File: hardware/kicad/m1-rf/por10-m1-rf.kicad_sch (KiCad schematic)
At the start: 17 parts, among them T1 1:5, U1 Si4735-D60-SSOP24, X1 32.768kHz

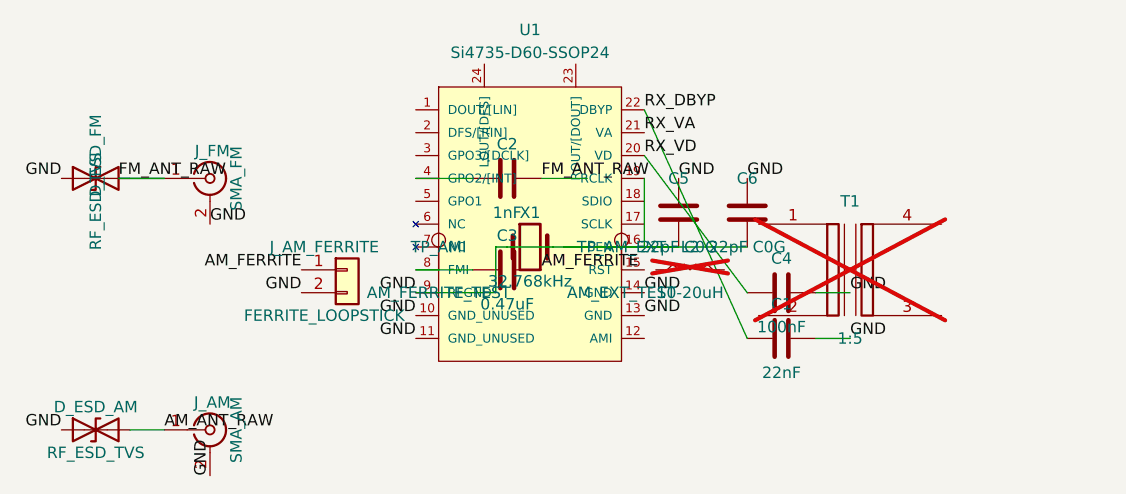
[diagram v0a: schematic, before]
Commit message: M1.3: add AM baseline bypass resistor
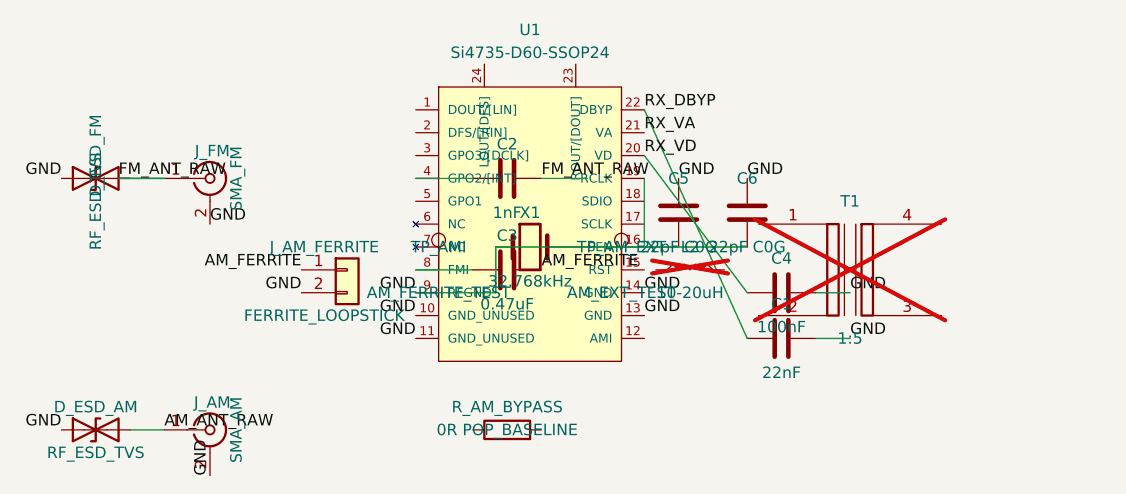
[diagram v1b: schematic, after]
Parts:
- added R_AM_BYPASS: 0R POP_BASELINE, symbol Device:R
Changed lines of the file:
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@@
     (effects (font (size 1.27 1.27)) (justify left bottom))
+  )
+  (symbol
+    (lib_id "Device:R")
+    (at 124.46 124.46 90)
+    (unit 1)
+    (exclude_from_sim no)
+    (in_bom yes)
+    (on_board yes)
+    (dnp no)
+    (property "Reference" "R_AM_BYPASS" (at 124.46 121.92 90) (effects (font (size 1.27 1.27))))
+    (property "Value" "0R POP_BASELINE" (at 124.46 124.46 90) (effects (font (size 1.27 1.27))))
+    (property "Footprint" "" (at 124.46 126.238 90) (effects (font (size 1.27 1.27)) (hide yes)))
+    (property "Datasheet" "~" (at 124.46 124.46 0) (effects (font (size 1.27 1.27)) (hide yes)))
+    (property "Description" "Q1 baseline 0-ohm bypass for external AM/SW matching experiments" (at 124.46 124.46 0) (effects (font (size 1.27 1.27)) (hide yes)))
+    (pin "1")
+    (pin "2")
+    (instances (project "por10-m1-rf" (path "/2b0f5db7-74f4-4a9a-bfc8-7bcbf6f10a13" (reference "R_AM_BYPASS") (unit 1))))
   )
   (sheet_instances

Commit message: M1.3: connect AM baseline bypass to external test node
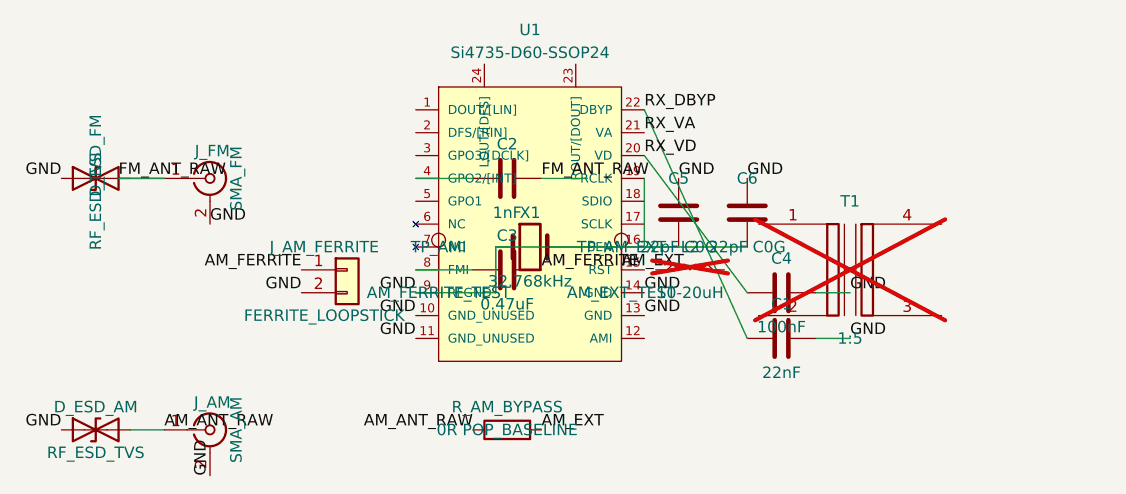
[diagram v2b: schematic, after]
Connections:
- net AM_ANT_RAW: now also R_AM_BYPASS.1
- net AM_EXT: now reaches TP_AM_EXT.1
- net AM_EXT: now also R_AM_BYPASS.2
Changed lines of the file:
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@@
     (instances (project "por10-m1-rf" (path "/2b0f5db7-74f4-4a9a-bfc8-7bcbf6f10a13" (reference "R_AM_BYPASS") (unit 1))))
+  )
+  (label "AM_ANT_RAW"
+    (at 120.65 124.46 180)
+    (effects (font (size 1.27 1.27)) (justify right bottom))
+  )
+  (label "AM_EXT"
+    (at 128.27 124.46 0)
+    (effects (font (size 1.27 1.27)) (justify left bottom))
+  )
+  (label "AM_EXT"
+    (at 137.16 106.68 0)
+    (effects (font (size 1.27 1.27)) (justify left bottom))
   )
   (sheet_instances

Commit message: M1.3: add selectable external AM link
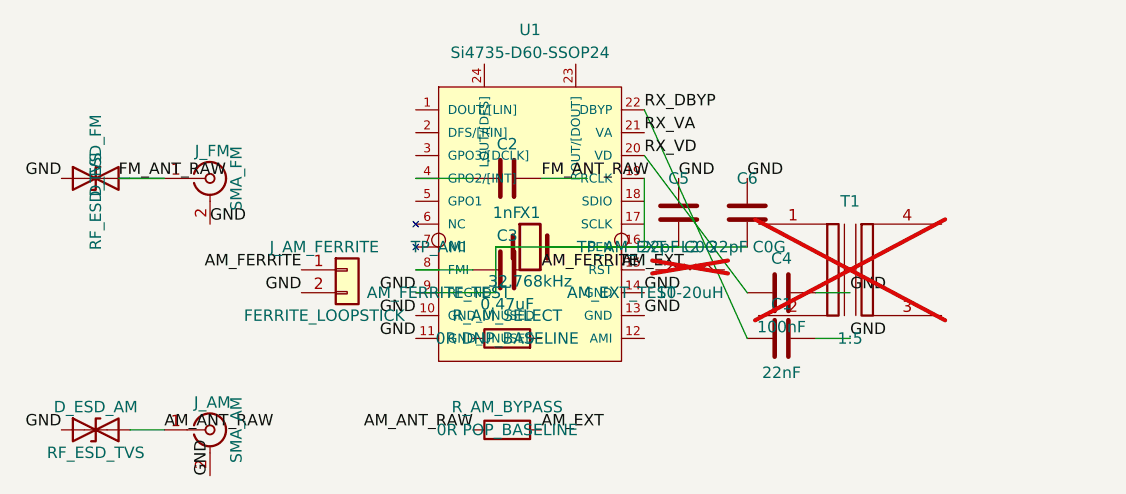
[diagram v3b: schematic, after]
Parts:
- added R_AM_SELECT: 0R DNP_BASELINE, symbol Device:R
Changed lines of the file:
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@@
     (effects (font (size 1.27 1.27)) (justify left bottom))
+  )
+  (symbol
+    (lib_id "Device:R")
+    (at 124.46 114.3 90)
+    (unit 1)
+    (exclude_from_sim no)
+    (in_bom yes)
+    (on_board yes)
+    (dnp no)
+    (property "Reference" "R_AM_SELECT" (at 124.46 111.76 90) (effects (font (size 1.27 1.27))))
+    (property "Value" "0R DNP_BASELINE" (at 124.46 114.3 90) (effects (font (size 1.27 1.27))))
+    (property "Footprint" "" (at 124.46 116.078 90) (effects (font (size 1.27 1.27)) (hide yes)))
+    (property "Datasheet" "~" (at 124.46 114.3 0) (effects (font (size 1.27 1.27)) (hide yes)))
+    (property "Description" "External AM/SW to AMI selection link; DNP in ferrite Q1 baseline" (at 124.46 114.3 0) (effects (font (size 1.27 1.27)) (hide yes)))
+    (pin "1")
+    (pin "2")
+    (instances (project "por10-m1-rf" (path "/2b0f5db7-74f4-4a9a-bfc8-7bcbf6f10a13" (reference "R_AM_SELECT") (unit 1))))
   )
   (sheet_instances

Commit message: M1.3: connect selectable external AM branch to AMI net
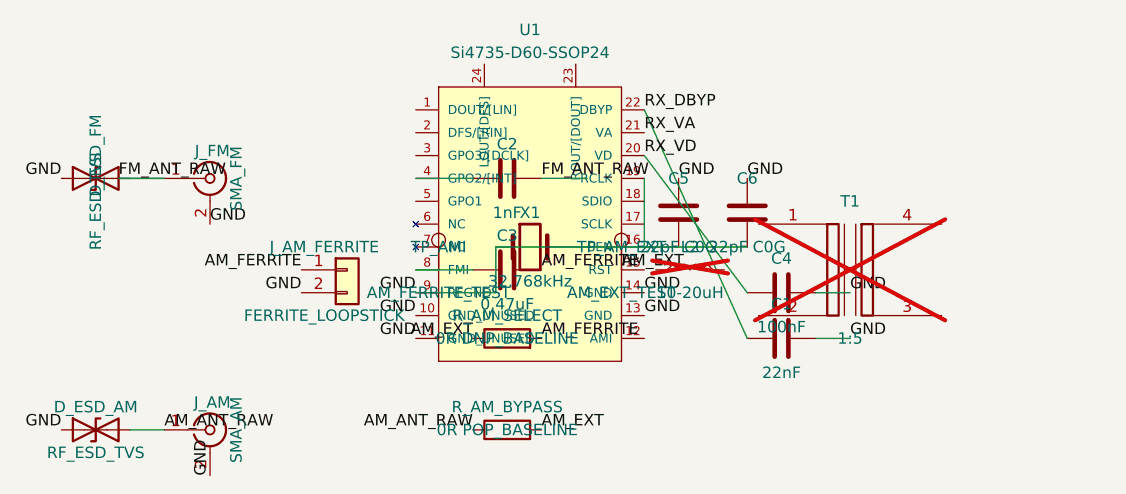
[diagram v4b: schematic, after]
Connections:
- net AM_EXT: now also R_AM_SELECT.1
- net AM_FERRITE: now also R_AM_SELECT.2
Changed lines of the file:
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@@
     (instances (project "por10-m1-rf" (path "/2b0f5db7-74f4-4a9a-bfc8-7bcbf6f10a13" (reference "R_AM_SELECT") (unit 1))))
+  )
+  (label "AM_EXT"
+    (at 120.65 114.3 180)
+    (effects (font (size 1.27 1.27)) (justify right bottom))
+  )
+  (label "AM_FERRITE"
+    (at 128.27 114.3 0)
+    (effects (font (size 1.27 1.27)) (justify left bottom))
   )
   (sheet_instances

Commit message: M1.3: connect optional L2 matching branch
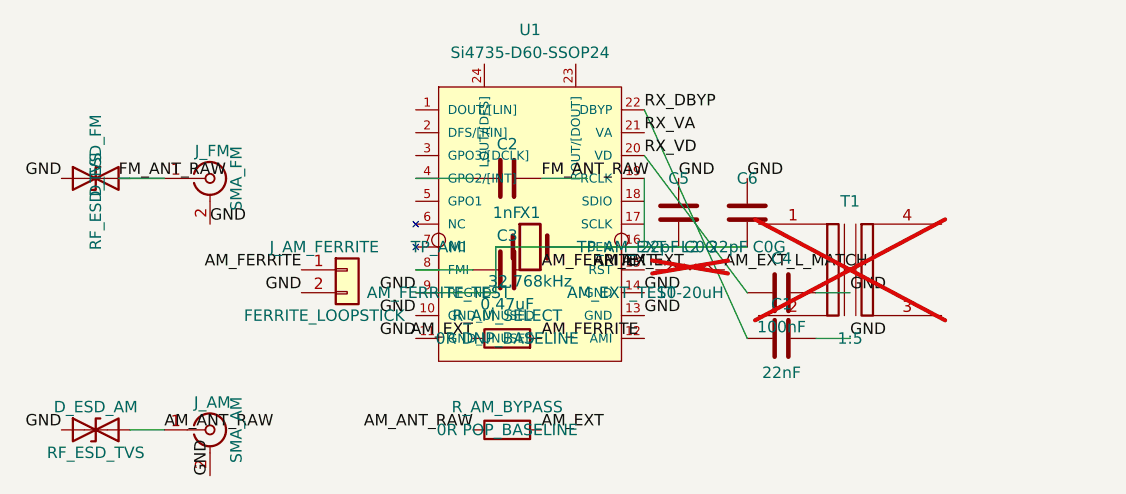
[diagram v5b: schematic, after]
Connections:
- net AM_EXT: now also L2.1
- net AM_EXT_L_MATCH: now reaches L2.2
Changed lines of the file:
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@@
+    (effects (font (size 1.27 1.27)) (justify left bottom))
+  )
+  (label "AM_EXT"
+    (at 140.97 106.68 180)
+    (effects (font (size 1.27 1.27)) (justify right bottom))
+  )
+  (label "AM_EXT_L_MATCH"
+    (at 148.59 106.68 0)
     (effects (font (size 1.27 1.27)) (justify left bottom))
   )

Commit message: M1.3: connect optional T1 matching branch
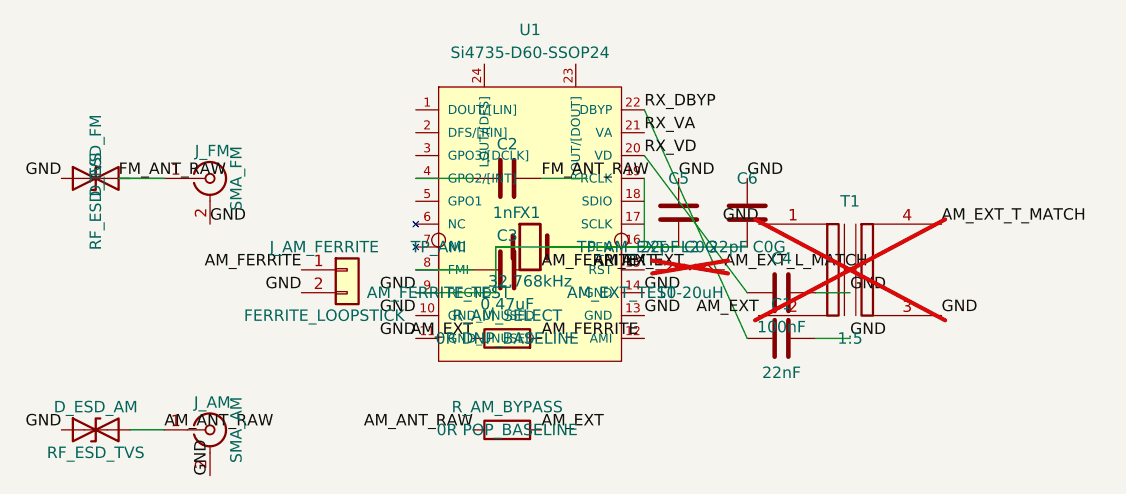
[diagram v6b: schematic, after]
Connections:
- net AM_EXT: now also T1.2 (AB)
- net GND: now also T1.1 (AA), T1.3 (SA)
- net AM_EXT_T_MATCH: now reaches T1.4 (SB)
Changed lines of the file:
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@@
+    (effects (font (size 1.27 1.27)) (justify left bottom))
+  )
+  (label "AM_EXT"
+    (at 152.4 111.76 180)
+    (effects (font (size 1.27 1.27)) (justify right bottom))
+  )
+  (label "GND"
+    (at 152.4 101.6 180)
+    (effects (font (size 1.27 1.27)) (justify right bottom))
+  )
+  (label "AM_EXT_T_MATCH"
+    (at 172.72 101.6 0)
+    (effects (font (size 1.27 1.27)) (justify left bottom))
+  )
+  (label "GND"
+    (at 172.72 111.76 0)
     (effects (font (size 1.27 1.27)) (justify left bottom))
   )

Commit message: M1.3: add optional AM matching selection links
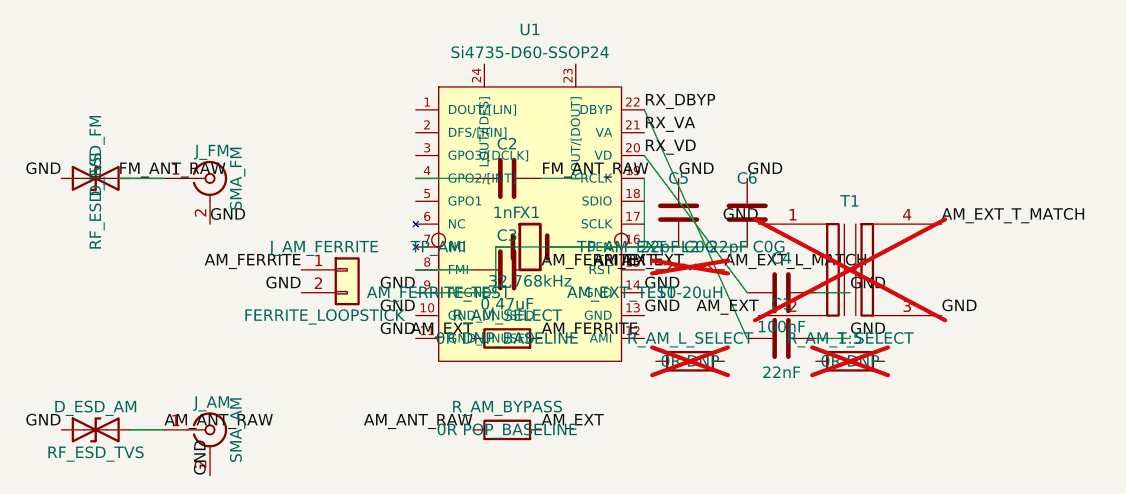
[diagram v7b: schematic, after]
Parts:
- added R_AM_L_SELECT: 0R DNP, symbol Device:R
- R_AM_T_SELECT: renamed from X1; value 32.768kHz -> 0R DNP; symbol Device:Crystal -> Device:R; now not fitted
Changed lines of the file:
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@@
     (effects (font (size 1.27 1.27)) (justify left bottom))
+  )
+  (symbol
+    (lib_id "Device:R")
+    (at 144.78 116.84 90)
+    (unit 1)
+    (exclude_from_sim no)
+    (in_bom yes)
+    (on_board yes)
+    (dnp yes)
+    (property "Reference" "R_AM_L_SELECT" (at 144.78 114.3 90) (effects (font (size 1.27 1.27))))
+    (property "Value" "0R DNP" (at 144.78 116.84 90) (effects (font (size 1.27 1.27))))
+    (property "Footprint" "" (at 144.78 118.618 90) (effects (font (size 1.27 1.27)) (hide yes)))
+    (property "Datasheet" "~" (at 144.78 116.84 0) (effects (font (size 1.27 1.27)) (hide yes)))
+    (property "Description" "Select optional L2 AM/SW matching path to AMI; mutually exclusive experiment link" (at 144.78 116.84 0) (effects (font (size 1.27 1.27)) (hide yes)))
+    (pin "1")
+    (pin "2")
+    (instances (project "por10-m1-rf" (path "/2b0f5db7-74f4-4a9a-bfc8-7bcbf6f10a13" (reference "R_AM_L_SELECT") (unit 1))))
+  )
+  (symbol
+    (lib_id "Device:R")
+    (at 162.56 116.84 90)
+    (unit 1)
+    (exclude_from_sim no)
+    (in_bom yes)
+    (on_board yes)
+    (dnp yes)
+    (property "Reference" "R_AM_T_SELECT" (at 162.56 114.3 90) (effects (font (size 1.27 1.27))))
+    (property "Value" "0R DNP" (at 162.56 116.84 90) (effects (font (size 1.27 1.27))))
+    (property "Footprint" "" (at 162.56 118.618 90) (effects (font (size 1.27 1.27)) (hide yes)))
+    (property "Datasheet" "~" (at 162.56 116.84 0) (effects (font (size 1.27 1.27)) (hide yes)))
+    (property "Description" "Select optional T1 AM/SW matching path to AMI; mutually exclusive experiment link" (at 162.56 116.84 0) (effects (font (size 1.27 1.27)) (hide yes)))
+    (pin "1")
+    (pin "2")
+    (instances (project "por10-m1-rf" (path "/2b0f5db7-74f4-4a9a-bfc8-7bcbf6f10a13" (reference "R_AM_T_SELECT") (unit 1))))
   )
   (sheet_instances

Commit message: M1.3: connect optional AM matching selectors
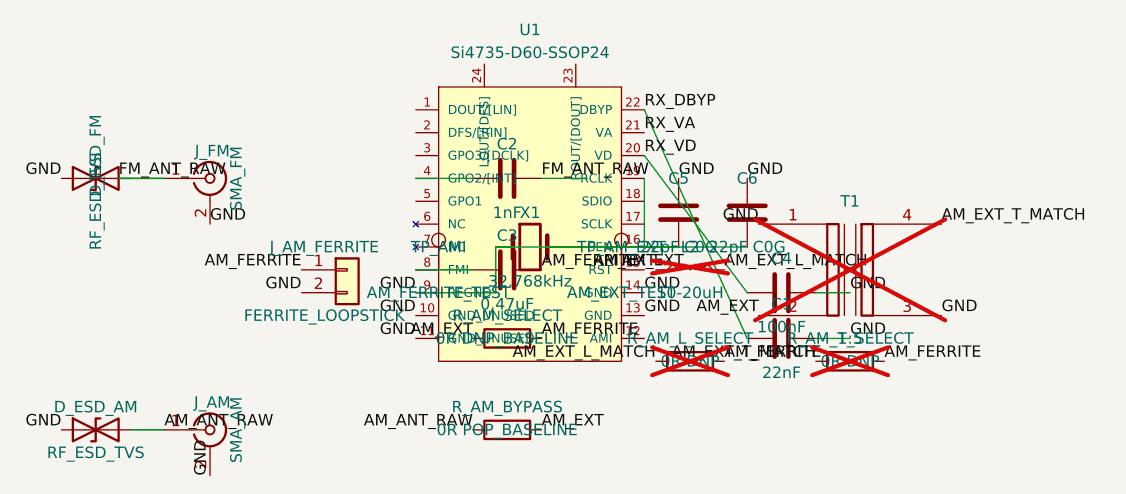
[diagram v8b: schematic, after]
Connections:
- net AM_EXT_L_MATCH: now also R_AM_L_SELECT.1
- net AM_EXT_T_MATCH: now also R_AM_T_SELECT.1
- net AM_FERRITE: now also R_AM_L_SELECT.2, R_AM_T_SELECT.2
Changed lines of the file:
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@@
     (instances (project "por10-m1-rf" (path "/2b0f5db7-74f4-4a9a-bfc8-7bcbf6f10a13" (reference "R_AM_T_SELECT") (unit 1))))
+  )
+  (label "AM_EXT_L_MATCH"
+    (at 140.97 116.84 180)
+    (effects (font (size 1.27 1.27)) (justify right bottom))
+  )
+  (label "AM_FERRITE"
+    (at 148.59 116.84 0)
+    (effects (font (size 1.27 1.27)) (justify left bottom))
+  )
+  (label "AM_EXT_T_MATCH"
+    (at 158.75 116.84 180)
+    (effects (font (size 1.27 1.27)) (justify right bottom))
+  )
+  (label "AM_FERRITE"
+    (at 166.37 116.84 0)
+    (effects (font (size 1.27 1.27)) (justify left bottom))
   )
   (sheet_instances
